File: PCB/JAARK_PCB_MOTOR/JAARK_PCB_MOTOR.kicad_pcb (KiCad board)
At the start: 2 copper layers, 90 x 90 mm, 34 parts, among them IC1 TPS564242DRLR, IC10 DRV8231DDAR, IC9 DRV8231DDAR, J1 Battery Terminal, J2 Morpho_x2_SSW-119-01-T-D, Q1 SSM3J334RLF, U1 4A

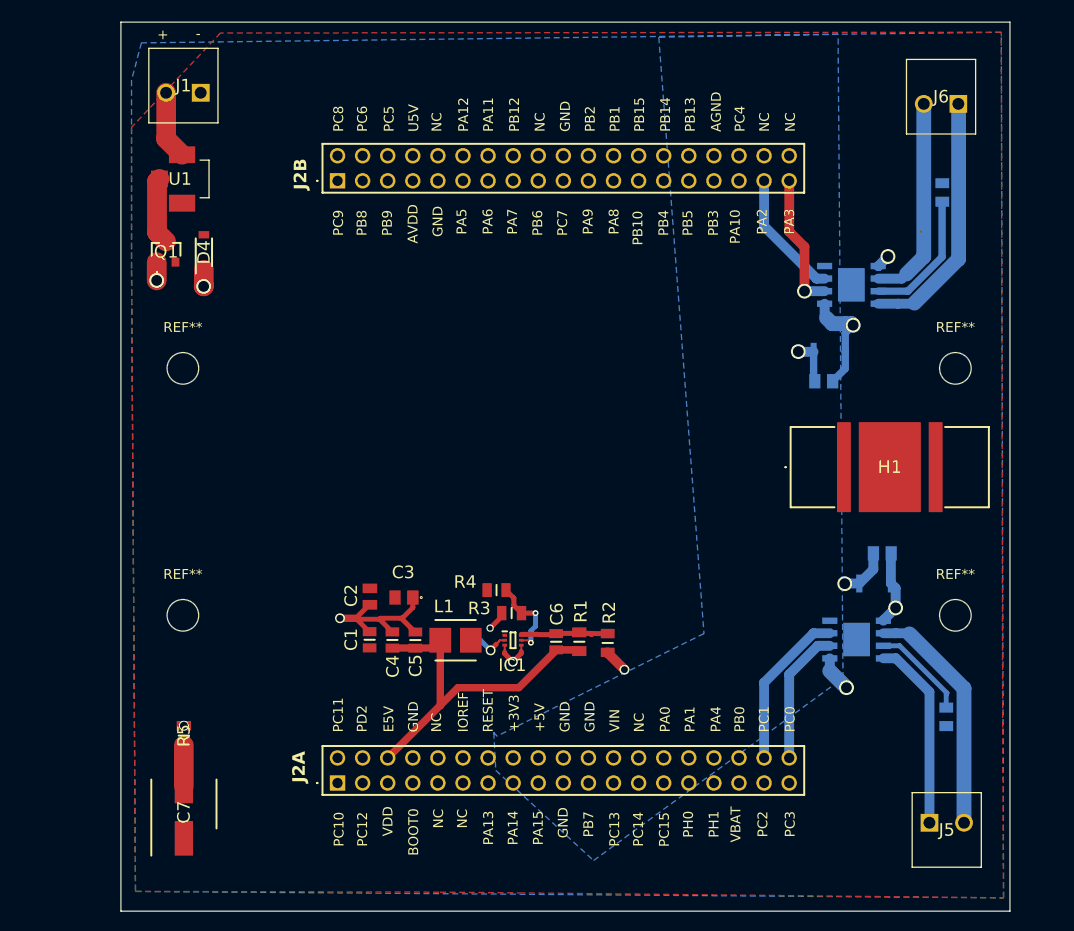
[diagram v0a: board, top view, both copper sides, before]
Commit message: More work on PCB, removed heatsink and then added mounting holes again
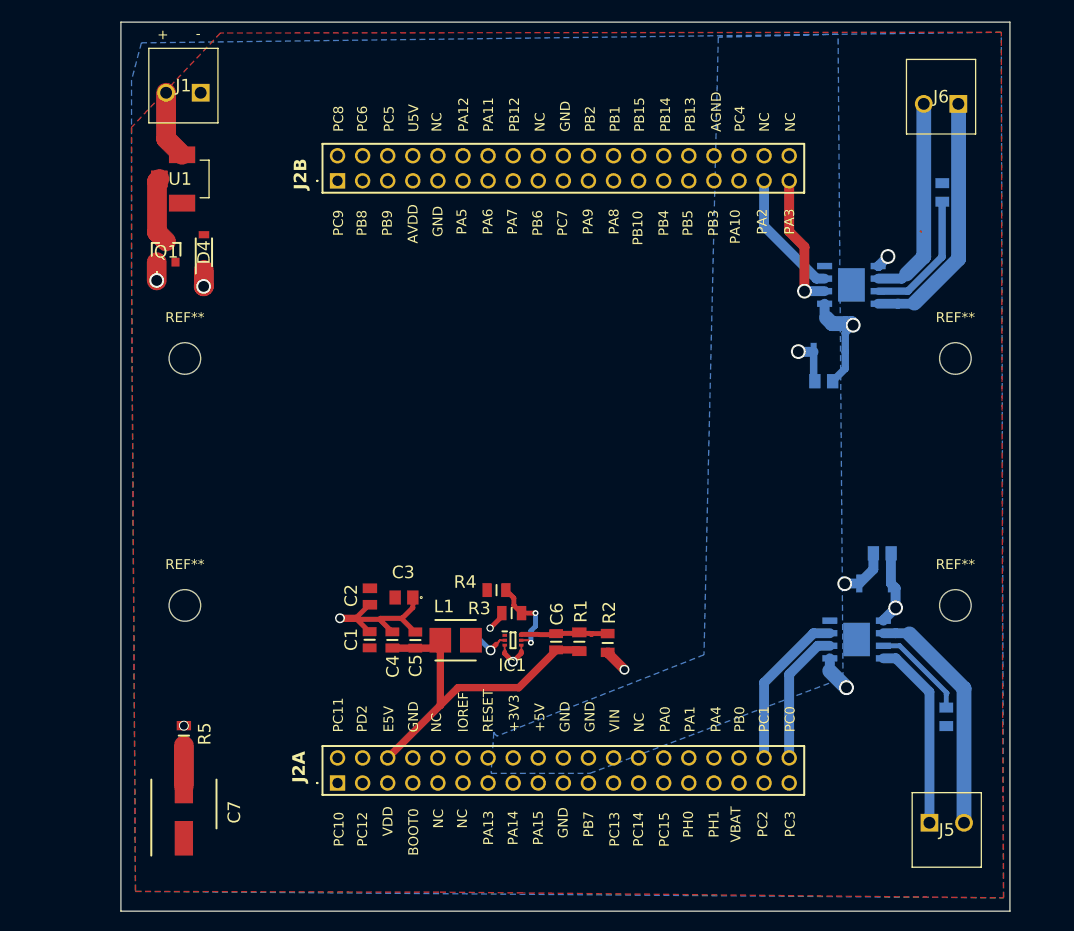
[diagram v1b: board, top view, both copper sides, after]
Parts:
- removed H1: V-1100-SMD_B-L, JAARK_lib:V1100SMDBL
- removed the REF** at (185.0, 80.0)
- removed the REF** at (185.0, 105.0)
- removed the REF** at (106.8, 105.0)
- removed the REF** at (106.8, 80.0)
- added REF**: MountingHole_3.2mm_M3, MountingHole:MountingHole_3.2mm_M3, F.Cu at (107.0, 104.0)
- added REF**: MountingHole_3.2mm_M3, MountingHole:MountingHole_3.2mm_M3, F.Cu at (185.0, 79.0)
- added REF**: MountingHole_3.2mm_M3, MountingHole:MountingHole_3.2mm_M3, F.Cu at (107.0, 79.0)
- added REF**: MountingHole_3.2mm_M3, MountingHole:MountingHole_3.2mm_M3, F.Cu at (185.0, 104.0)
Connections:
- U1 pad 1: Net-(J1-Pad2) -> Net-(Q1-D)
- U1 pad 2: Net-(Q1-D) -> Net-(J1-Pad2)
- U1 pad 3: (no net) -> unconnected-(U1-Pad3)
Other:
- board text added: "78mm"
- board text removed: "78.1mm"

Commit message: Fixed motor positioning.
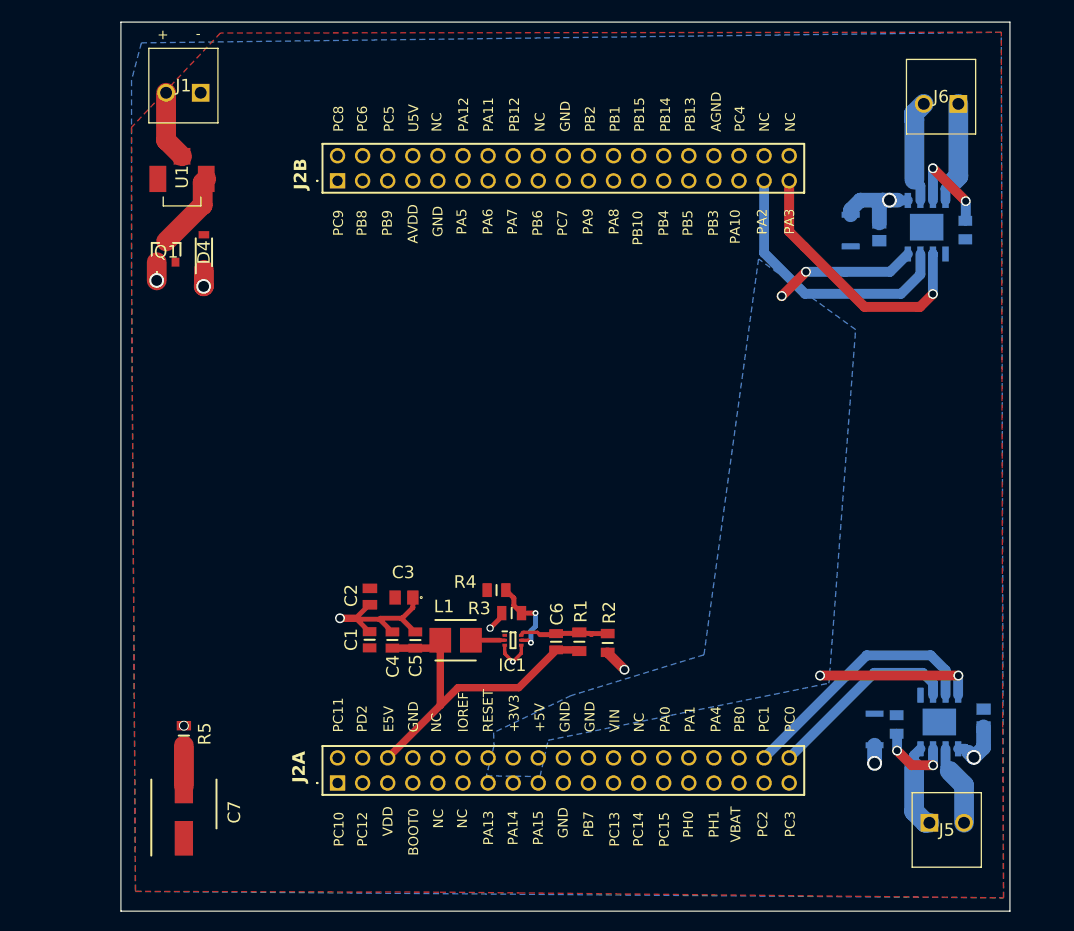
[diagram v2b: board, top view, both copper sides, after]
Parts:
- removed REF** (x4): MountingHole_3.2mm_M3, MountingHole:MountingHole_3.2mm_M3
- moved C13 19.6 mm to (187.8, 115.4), turned to 90 degrees
- moved C15 16.1 mm to (177.3, 66.2), turned to -90 degrees
- moved C14 14.8 mm to (176.8, 116.5), turned to -90 degrees
- moved C12 12.5 mm to (174.4, 66.0), turned to 90 degrees
- moved IC9 11.8 mm to (183.4, 115.8), turned to -90 degrees
- moved IC10 9.60 mm to (182.1, 65.7), turned to 90 degrees
- moved R10 5.08 mm to (179.1, 116.0), turned to 90 degrees
- moved R11 4.46 mm to (186.0, 66.0), turned to -90 degrees
- turned U1 to 90 degrees
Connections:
- J2 pad B20: unconnected-(J2B-GND-PadB20) -> GND
- J2 pad B32: unconnected-(J2B-AGND-PadB32) -> GND
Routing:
- net +3V3: track 0.00 -> 30.5 mm, vias 0 -> 4
- net GND: track 48.6 -> 28.6 mm, vias 10 -> 7
- net Net-(IC9-OUT1): track 24.1 -> 8.26 mm
- net Net-(IC10-OUT2): track 25.8 -> 10.4 mm
- net /IN4: track 12.9 -> 27.7 mm
- net /IN3: track 13.9 -> 27.4 mm
- net Net-(IC9-OUT2): track 19.3 -> 8.63 mm
- net Net-(IC10-OUT1): track 21.0 -> 10.5 mm
- net /IN2: track 16.3 -> 25.8 mm
- net /IN1: track 13.8 -> 19.8 mm
- net Net-(IC10-ISEN): track 13.5 -> 9.82 mm, vias 0 -> 2
- net +12V: track 13.5 -> 16.4 mm
- net Net-(IC9-ISEN): track 9.91 -> 7.66 mm, vias 0 -> 2
- net Net-(Q1-D): track 6.80 -> 8.04 mm
- net Net-(IC1-FB): track 8.70 -> 9.64 mm
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
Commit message: Bluetooth module
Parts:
- added J3: HC-05, JAARK_lib:PPPC061LGBNRC, F.Cu at (104.8, 90.6)
- added Q3: BC237B, JAARK_lib:TO-92__TO-226_, F.Cu at (119.0, 83.0)
- added R6: 4.3kR, Resistor_THT:R_Axial_DIN0207_L6.3mm_D2.5mm_P10.16mm_Horizontal, F.Cu at (136.0, 84.1)
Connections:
- J2 pad A34: unconnected-(J2A-PB0-PadA34) -> /P_HC
- J2 pad A4: unconnected-(J2A-PD2-PadA4) -> /ST_HC
- J2 pad B1: unconnected-(J2B-PC9-PadB1) -> /EN_HC
- J2 pad B21: unconnected-(J2B-PA9-PadB21) -> /TX_HC
- J2 pad B33: unconnected-(J2B-PA10-PadB33) -> /RX_HC
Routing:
- net /RX_HC: track 0.00 -> 69.5 mm, vias 0 -> 1
- net /TX_HC: track 0.00 -> 53.2 mm, vias 0 -> 1
- net /P_HC: track 0.00 -> 52.5 mm, vias 0 -> 1
- net +5V: track 36.0 -> 86.7 mm
- net /ST_HC: track 0.00 -> 37.2 mm
- net /EN_HC: track 0.00 -> 24.6 mm
- net Net-(J3-GND): track 0.00 -> 14.2 mm
- net GND: track 28.6 -> 37.6 mm, vias 7 -> 8
- net Net-(Q3-B): track 0.00 -> 5.61 mm

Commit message: Motor PCB finished?
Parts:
- added J4: Metal Detector, JAARK_lib:1984617, F.Cu at (182.6, 93.8)
- added M3_1: M3_1, MountingHole:MountingHole_3.2mm_M3, F.Cu at (185.0, 82.0)
- added M3_2: M3_2, MountingHole:MountingHole_3.2mm_M3, F.Cu at (185.0, 102.0)
- added M3_3: M3_3, MountingHole:MountingHole_3.2mm_M3, F.Cu at (107.0, 106.0)
- added M3_4: M3_4, MountingHole:MountingHole_3.2mm_M3, F.Cu at (107.0, 78.0)
- R2: footprint JAARK_lib:RESC2012X60N -> JAARK_lib:RESC2012X65N
- moved J3 8.41 mm to (104.9, 99.0)
- moved R5 6.77 mm to (104.5, 123.5)
- moved Q3 5.72 mm to (117.2, 88.4)
- moved C7 5.59 mm to (107.2, 130.5), turned to 180 degrees
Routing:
- net /EN_HC: track 24.6 -> 35.7 mm
- net +5V: track 86.7 -> 75.9 mm
- net Net-(Q3-B): track 5.61 -> 11.9 mm
- net /RX_HC: track 69.5 -> 73.7 mm
- net /TX_HC: track 53.2 -> 57.1 mm
- net /ST_HC: track 37.2 -> 33.7 mm
- net Net-(C7--): track 4.10 -> 6.04 mm
- net Net-(J3-GND): track 14.2 -> 16.0 mm
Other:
- board text added: "17mm"
- board text added: "<-|"
- board text added: "[J]onart B. [A]bdul Q. [A]ffaan A. [R]ohan F. [K]arim K."

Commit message: added test points
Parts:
- removed R5: 20kR, JAARK_lib:RESC2012X50N
- added 12V: 12V, TestPoint:TestPoint_Pad_1.5x1.5mm, F.Cu at (104.5, 115.8)
- added 3V3: 3.3V, TestPoint:TestPoint_Pad_1.5x1.5mm, F.Cu at (111.0, 115.8)
- added 5V: 5V, TestPoint:TestPoint_Pad_1.5x1.5mm, F.Cu at (107.8, 112.5)
- added C8: 0.1uF, JAARK_lib:C0805, F.Cu at (111.9, 111.4)
- added C9: 0.1uF, JAARK_lib:C0805, B.Cu at (111.0, 119.5)
- added GND: GND, TestPoint:TestPoint_Pad_1.5x1.5mm, F.Cu at (107.8, 115.8)
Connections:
- C7 pad 2: Net-(C7--) -> GND
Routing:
- net +3V3: track 30.5 -> 68.5 mm, vias 4 -> 7
- net +5V: track 75.9 -> 87.9 mm
- net GND: track 37.6 -> 48.9 mm, vias 8 -> 10
- net Net-(C7--): track 6.04 -> 0.00 mm
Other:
- board text added: "20mm"
- board text added: "28mm"
- board text removed: "17mm"
- board text removed: "25mm"

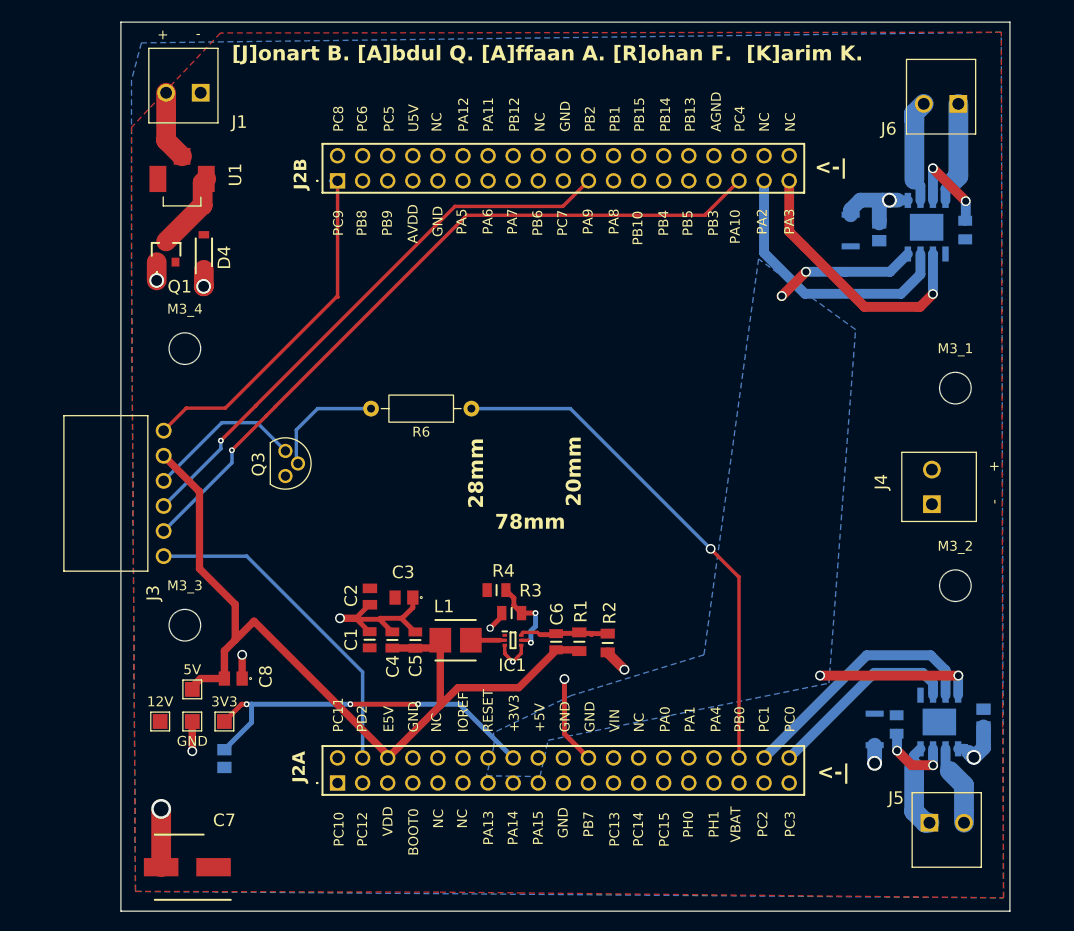
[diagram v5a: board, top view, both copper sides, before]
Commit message: JLCPCB compatibility
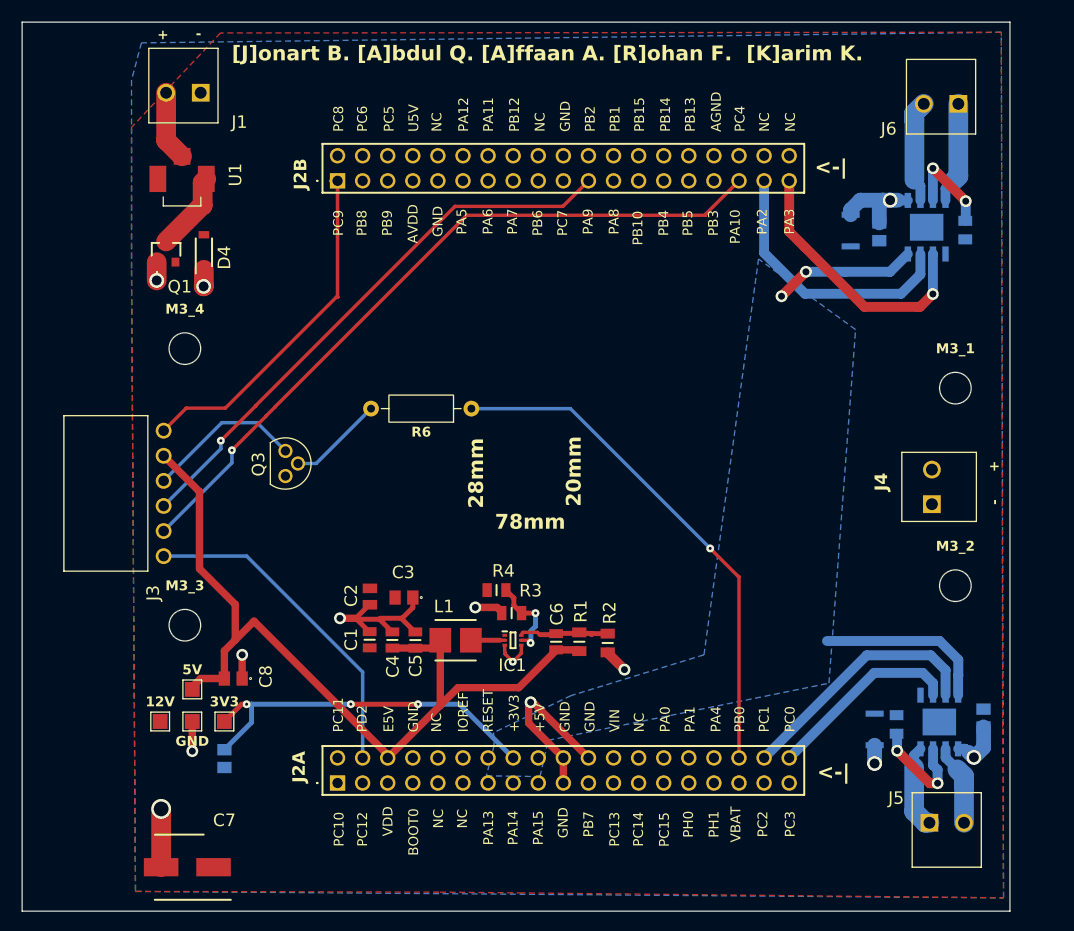
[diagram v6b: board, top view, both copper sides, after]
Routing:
- net GND: track 48.9 -> 58.9 mm
- net Net-(IC9-ISEN): track 7.66 -> 10.9 mm
- net Net-(Q3-B): track 11.9 -> 9.94 mm
- net +3V3: track 68.5 -> 70.2 mm, vias 7 -> 5
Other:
- board size 90 x 90 mm -> 100 x 90 mm

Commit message: Final prototype of PCB
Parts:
- removed 12V: 12V, TestPoint:TestPoint_Pad_1.5x1.5mm
- removed 5V: 5V, TestPoint:TestPoint_Pad_1.5x1.5mm
- removed GND: GND, TestPoint:TestPoint_Pad_1.5x1.5mm
- added 12V1: 12V, TestPoint:TestPoint_Pad_1.5x1.5mm, F.Cu at (104.4, 115.7)
- added 5V1: 5V, TestPoint:TestPoint_Pad_1.5x1.5mm, F.Cu at (107.8, 112.5)
- added G***: LOGO, JAARK_lib:jaark_big, F.Cu at (145.4, 76.0)
- added GND1: GND, TestPoint:TestPoint_Pad_1.5x1.5mm, F.Cu at (105.6, 64.2)
- added J7: Metal Detector, JAARK_lib:1984617, F.Cu at (181.4, 86.8)
- C9: moved to F.Cu
- U1: value 4A -> 3568; footprint JAARK_lib:3586TR -> JAARK_lib:3568
- moved M3_1 18.0 mm to (167.0, 82.0)
- moved M3_2 18.0 mm to (167.0, 102.0)
- moved D4 12.1 mm to (99.6, 60.5)
- moved Q1 12.1 mm to (95.8, 60.5)
- moved J1 9.77 mm to (98.8, 52.1)
- moved U1 8.08 mm to (106.9, 52.8), turned to 0 degrees
- moved J4 8.05 mm to (181.6, 101.7)
- moved C9 1.62 mm to (110.9, 121.1)
- moved R4 1.45 mm to (140.0, 102.6), turned to 180 degrees
- moved R3 0.09 mm to (140.0, 104.8), turned to 0 degrees
- moved 3V3 0.05 mm to (111.0, 115.7)
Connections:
- IC10 pad 2: /IN3 -> /IN4
- IC10 pad 3: /IN4 -> /IN3
- R3 pad 1: Net-(IC1-EN) -> +12V
- R3 pad 2: GND -> Net-(IC1-EN)
- R4 pad 1: +12V -> Net-(IC1-EN)
- R4 pad 2: Net-(IC1-EN) -> GND
- U1 pad 1: Net-(Q1-D) -> Net-(J1-Pad2)
- U1 pad 3: unconnected-(U1-Pad3) -> Net-(Q1-D)
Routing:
- net +5V: track 87.9 -> 143.7 mm, vias 0 -> 2
- net Net-(Q1-D): track 8.04 -> 34.1 mm, vias 0 -> 1
- net GND: track 58.9 -> 47.6 mm
- net +3V3: track 70.2 -> 59.6 mm
- net Net-(J1-Pad2): track 7.10 -> 17.1 mm
- net /IN3: track 27.4 -> 22.7 mm, vias 1 -> 0
- net /IN4: track 27.7 -> 29.8 mm
- net Net-(IC1-EN): track 8.68 -> 7.88 mm
- net /P_HC: vias 1 -> 0
- added copper zone on F.Cu, net +3V3
- removed copper zone on B.Cu, net +3V3
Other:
- outline, holes or cut-outs redrawn
- board text added: "12V"
- board text added: "12V Power Supply"
- board text added: "12V to 5V"
- board text added: "5V"
- board text added: "HC-05 Module"
- board text added: "Jonart Abdul Affaan Rohan Karim"
- board text added: "Motor 1"
- board text added: "Motor 2"
- board text removed: "[J]onart B. [A]bdul Q. [A]ffaan A. [R]ohan F. [K]arim K."
